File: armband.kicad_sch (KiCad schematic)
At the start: 35 parts, among them IC1 STM32MP157AAB3, IC7 S40FC004C1B2C00000, IC9 NXS0506UPZ, J2 Conn_01x02, J3 MEM2075-00-140-01-A, SW1 SW_MEC_5G, SW2 SW_MEC_5G

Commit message: first power management layout iteration, added footprints and values to parts that had none
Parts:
- C1, C2: footprint Capacitor_SMD:C_0603_1608Metric -> Capacitor_SMD:C_0402_1005Metric
- C27, C28, C66: footprint (none) -> Capacitor_SMD:C_0402_1005Metric
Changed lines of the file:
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@@
       (effects (font (size 1.27 1.27)) (justify left))
     )
-    (property "Footprint" "" (at 344.17 86.36 0)
+    (property "Footprint" "Capacitor_SMD:C_0402_1005Metric" (at 344.17 86.36 0)
       (effects (font (size 1.27 1.27)) hide)
     )
@@
       (effects (font (size 1.27 1.27)) (justify left))
     )
-    (property "Footprint" "" (at 394.97 121.92 0)
+    (property "Footprint" "Capacitor_SMD:C_0402_1005Metric" (at 394.97 121.92 0)
       (effects (font (size 1.27 1.27)) hide)
     )
@@
       (effects (font (size 1.27 1.27)) (justify left))
     )
-    (property "Footprint" "Capacitor_SMD:C_0603_1608Metric" (at 294.64 46.99 0)
+    (property "Footprint" "Capacitor_SMD:C_0402_1005Metric" (at 294.64 46.99 0)
       (effects (font (size 1.27 1.27)) hide)
     )
@@
       (effects (font (size 1.27 1.27)) (justify left))
     )
-    (property "Footprint" "Capacitor_SMD:C_0603_1608Metric" (at 318.77 46.99 0)
+    (property "Footprint" "Capacitor_SMD:C_0402_1005Metric" (at 318.77 46.99 0)
       (effects (font (size 1.27 1.27)) hide)
     )
@@
       (effects (font (size 1.27 1.27)) (justify left))
     )
-    (property "Footprint" "" (at 392.43 55.88 0)
+    (property "Footprint" "Capacitor_SMD:C_0402_1005Metric" (at 392.43 55.88 0)
       (effects (font (size 1.27 1.27)) hide)
     )
@@
   )
   (symbol (lib_id "ARMband:S40FC004C1B2C00000") (at 384.81 34.29 0) (unit 1)
-    (in_bom yes) (on_board no) (dnp yes) (fields_autoplaced)
+    (in_bom yes) (on_board yes) (dnp yes) (fields_autoplaced)
     (property "Reference" "IC7" (at 364.49 27.5209 0)
       (effects (font (size 1.27 1.27)))

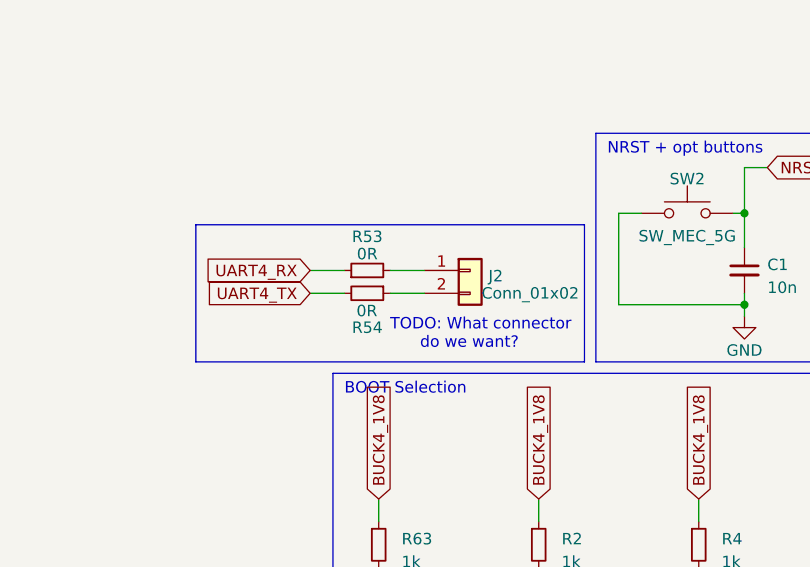
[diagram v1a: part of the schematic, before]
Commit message: Add missing footprints to components
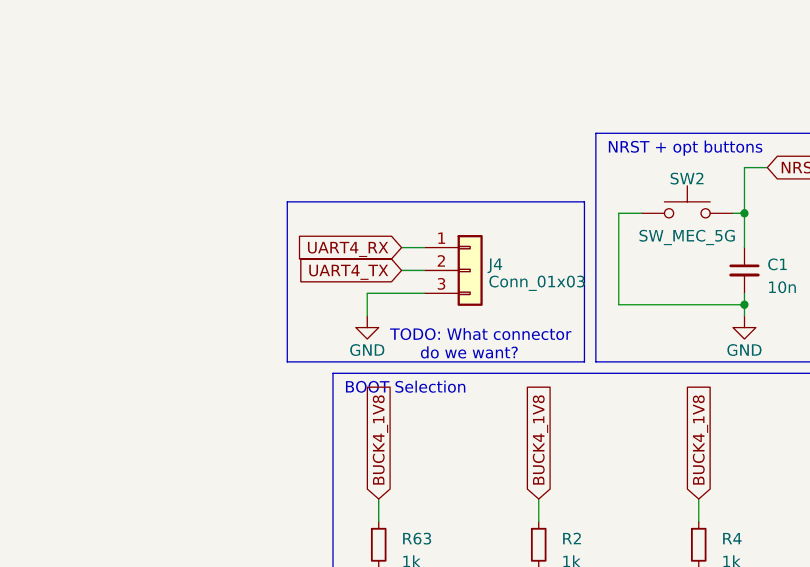
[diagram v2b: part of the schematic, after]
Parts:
- removed J2: Conn_01x02, symbol Connector_Generic:Conn_01x02
- removed R53, R54: 0R, Resistor_SMD:R_0201_0603Metric_Pad0.64x0.40mm_HandSolder, symbol Device:R_Small
- added J4: Conn_01x03, Connector_PinHeader_2.54mm:PinHeader_1x03_P2.54mm_Vertical, symbol Connector_Generic:Conn_01x03
- R55: footprint (none) -> Resistor_SMD:R_0402_1005Metric
- SW1, SW2: footprint (none) -> ARMband:SW-SMD_4P-L2.6-W1.6-P0.75-LS3.0; LCSC (none) -> C913778
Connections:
- net GND: now also J4.3 (Pin_3)
- net UART4_RX: now also J4.1 (Pin_1)
- net UART4_TX: now also J4.2 (Pin_2)
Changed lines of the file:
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@@
     (stroke (width 0) (type default))
   )
-  (wire (pts (xy 255.27 49.53) (xy 259.08 49.53))
-    (stroke (width 0) (type default))
-  )
-  (wire (pts (xy 246.38 46.99) (xy 250.19 46.99))
-    (stroke (width 0) (type default))
-  )
   (polyline (pts (xy 278.13 31.75) (xy 328.93 31.75))
     (stroke (width 0) (type default))
@@
     (stroke (width 0) (type default))
   )
-  (wire (pts (xy 255.27 46.99) (xy 259.08 46.99))
+  (wire (pts (xy 256.54 44.45) (xy 259.08 44.45))
     (stroke (width 0) (type default))
   )
@@
     (stroke (width 0) (type default))
   )
-  (wire (pts (xy 246.38 49.53) (xy 250.19 49.53))
+  (wire (pts (xy 256.54 46.99) (xy 259.08 46.99))
     (stroke (width 0) (type default))
   )
@@
     (stroke (width 0) (type default))
   )
+  (wire (pts (xy 252.73 49.53) (xy 252.73 52.07))
+    (stroke (width 0) (type default))
+  )
   (wire (pts (xy 384.81 67.31) (xy 384.81 69.85))
     (stroke (width 0) (type default))
@@
     (stroke (width 0) (type default))
   )
+  (wire (pts (xy 259.08 49.53) (xy 252.73 49.53))
+    (stroke (width 0) (type default))
+  )
   (wire (pts (xy 332.74 113.03) (xy 332.74 128.27))
     (stroke (width 0) (type default))
@@
     (fill (type none))
   )
-  (rectangle (start 233.68 41.91) (end 276.86 57.15)
+  (rectangle (start 243.84 39.37) (end 276.86 57.15)
     (stroke (width 0) (type default))
     (fill (type none))
@@
     (effects (font (size 1.27 1.27)) (justify left bottom))
   )
-  (text "TODO: What connector\n      do we want?" (at 255.27 55.88 0)
+  (text "TODO: What connector\n      do we want?" (at 255.27 57.15 0)
     (effects (font (size 1.27 1.27)) (justify left bottom))
   )
@@
     )
   )
-  (global_label "UART4_RX" (shape input) (at 246.38 46.99 180) (fields_autoplaced)
+  (global_label "UART4_RX" (shape input) (at 256.54 44.45 180) (fields_autoplaced)
     (effects (font (size 1.27 1.27)) (justify right))
-    (property "Intersheetrefs" "${INTERSHEET_REFS}" (at 234.1609 46.99 0)
+    (property "Intersheetrefs" "${INTERSHEET_REFS}" (at 244.3209 44.45 0)
       (effects (font (size 1.27 1.27)) (justify right) hide)
     )
@@
     )
   )
-  (global_label "UART4_TX" (shape input) (at 246.38 49.53 180) (fields_autoplaced)
+  (global_label "UART4_TX" (shape input) (at 256.54 46.99 180) (fields_autoplaced)
     (effects (font (size 1.27 1.27)) (justify right))
-    (property "Intersheetrefs" "${INTERSHEET_REFS}" (at 234.4633 49.53 0)
+    (property "Intersheetrefs" "${INTERSHEET_REFS}" (at 244.6233 46.99 0)
       (effects (font (size 1.27 1.27)) (justify right) hide)
     )
@@
       (effects (font (size 1.27 1.27)))
     )
-    (property "Footprint" "" (at 346.71 134.62 0)
+    (property "Footprint" "Resistor_SMD:R_0402_1005Metric" (at 346.71 134.62 0)
       (effects (font (size 1.27 1.27)) hide)
     )
@@
     )
   )
+  (symbol (lib_id "Connector_Generic:Conn_01x03") (at 264.16 46.99 0) (unit 1)
+    (in_bom yes) (on_board yes) (dnp no) (fields_autoplaced)
+    (property "Reference" "J4" (at 266.192 46.3463 0)
+      (effects (font (size 1.27 1.27)) (justify left))
+    )
+    (property "Value" "Conn_01x03" (at 266.192 48.2673 0)
+      (effects (font (size 1.27 1.27)) (justify left))
+    )
+    (property "Footprint" "Connector_PinHeader_2.54mm:PinHeader_1x03_P2.54mm_Vertical" (at 264.16 46.99 0)
+      (effects (font (size 1.27 1.27)) hide)
+    )
+    (property "Datasheet" "~" (at 264.16 46.99 0)
+      (effects (font (size 1.27 1.27)) hide)
+    )
+    (pin "1")
+    (pin "2")
+    (pin "3")
+    (instances
+      (project "armband"
+        (path "/017c50c6-333c-4d31-ad5a-278994a09b14"
+          (reference "J4") (unit 1)
+        )
+      )
+    )
+  )
   (symbol (lib_id "Device:R_Small") (at 36.83 62.23 90) (unit 1)
     (in_bom yes) (on_board yes) (dnp no)
@@
       (effects (font (size 1.27 1.27)))
     )
-    (property "Footprint" "" (at 312.42 35.56 0)
+    (property "Footprint" "ARMband:SW-SMD_4P-L2.6-W1.6-P0.75-LS3.0" (at 312.42 35.56 0)
       (effects (font (size 1.27 1.27)) hide)
     )
@@
       (effects (font (size 1.27 1.27)) hide)
     )
+    (property "LCSC" "C913778" (at 312.42 40.64 0)
+      (effects (font (size 1.27 1.27)) hide)
+    )
     (pin "1")
     (pin "3")
@@
     )
   )
-  (symbol (lib_id "Connector_Generic:Conn_01x02") (at 264.16 46.99 0) (unit 1)
-    (in_bom yes) (on_board yes) (dnp no)
-    (property "Reference" "J2" (at 266.192 47.6163 0)
-      (effects (font (size 1.27 1.27)) (justify left))
-    )
-    (property "Value" "Conn_01x02" (at 265.43 49.53 0)
-      (effects (font (size 1.27 1.27)) (justify left))
-    )
-    (property "Footprint" "" (at 264.16 46.99 0)
-      (effects (font (size 1.27 1.27)) hide)
-    )
-    (property "Datasheet" "~" (at 264.16 46.99 0)
-      (effects (font (size 1.27 1.27)) hide)
-    )
-    (pin "1")
-    (pin "2")
-    (instances
-      (project "armband"
-        (path "/017c50c6-333c-4d31-ad5a-278994a09b14"
-          (reference "J2") (unit 1)
-        )
-      )
-    )
-  )
   (symbol (lib_id "Device:C_Small") (at 318.77 46.99 0) (unit 1)
     (in_bom yes) (on_board yes) (dnp no) (fields_autoplaced)
@@
     )
   )
+  (symbol (lib_name "GND_1") (lib_id "power:GND") (at 252.73 52.07 0) (mirror y) (unit 1)
+    (in_bom yes) (on_board yes) (dnp no)
+    (property "Reference" "#PWR01" (at 252.73 58.42 0)
+      (effects (font (size 1.27 1.27)) hide)
+    )
+    (property "Value" "GND" (at 252.73 55.88 0)
+      (effects (font (size 1.27 1.27)))
+    )
+    (property "Footprint" "" (at 252.73 52.07 0)
+      (effects (font (size 1.27 1.27)) hide)
+    )
+    (property "Datasheet" "" (at 252.73 52.07 0)
+      (effects (font (size 1.27 1.27)) hide)
+    )
+    (pin "1")
+    (instances
+      (project "armband"
+        (path "/017c50c6-333c-4d31-ad5a-278994a09b14/5731d22b-18c2-4920-9f80-2a6ce209edf2"
+          (reference "#PWR01") (unit 1)
+        )
+        (path "/017c50c6-333c-4d31-ad5a-278994a09b14"
+          (reference "#PWR066") (unit 1)
+        )
+      )
+    )
+  )
   (symbol (lib_id "Device:R_Small") (at 254 87.63 0) (unit 1)
     (in_bom yes) (on_board yes) (dnp no) (fields_autoplaced)
@@
       (effects (font (size 1.27 1.27)))
     )
-    (property "Footprint" "" (at 288.29 35.56 0)
+    (property "Footprint" "ARMband:SW-SMD_4P-L2.6-W1.6-P0.75-LS3.0" (at 288.29 35.56 0)
       (effects (font (size 1.27 1.27)) hide)
     )
@@
       (effects (font (size 1.27 1.27)) hide)
     )
+    (property "LCSC" "C913778" (at 288.29 40.64 0)
+      (effects (font (size 1.27 1.27)) hide)
+    )
     (pin "1")
     (pin "3")
@@
     )
   )
-  (symbol (lib_id "Device:R_Small") (at 252.73 49.53 270) (unit 1)
-    (in_bom yes) (on_board yes) (dnp no)
-    (property "Reference" "R54" (at 252.73 53.34 90)
-      (effects (font (size 1.27 1.27)))
-    )
-    (property "Value" "0R" (at 252.6899 51.4872 90)
-      (effects (font (size 1.27 1.27)))
-    )
-    (property "Footprint" "Resistor_SMD:R_0201_0603Metric_Pad0.64x0.40mm_HandSolder" (at 252.73 49.53 0)
-      (effects (font (size 1.27 1.27)) hide)
-    )
-    (property "Datasheet" "~" (at 252.73 49.53 0)
-      (effects (font (size 1.27 1.27)) hide)
-    )
-    (property "MFN" "" (at 252.73 49.53 0)
-      (effects (font (size 1.27 1.27)) hide)
-    )
-    (pin "1")
-    (pin "2")
-    (instances
-      (project "armband"
-        (path "/017c50c6-333c-4d31-ad5a-278994a09b14"
-          (reference "R54") (unit 1)
-        )
-      )
-    )
-  )
   (symbol (lib_id "Device:R_Small") (at 313.69 83.82 0) (mirror y) (unit 1)
     (in_bom yes) (on_board yes) (dnp no)
@@
         )
       )
-    )
-  )
-  (symbol (lib_id "Device:R_Small") (at 252.73 46.99 90) (unit 1)
-    (in_bom yes) (on_board yes) (dnp no) (fields_autoplaced)
-    (property "Reference" "R53" (at 252.73 43.2435 90)
-      (effects (font (size 1.27 1.27)))
-    )
-    (property "Value" "0R" (at 252.73 45.1645 90)
-      (effects (font (size 1.27 1.27)))
-    )
-    (property "Footprint" "Resistor_SMD:R_0201_0603Metric_Pad0.64x0.40mm_HandSolder" (at 252.73 46.99 0)
-      (effects (font (size 1.27 1.27)) hide)
-    )
-    (property "Datasheet" "~" (at 252.73 46.99 0)
-      (effects (font (size 1.27 1.27)) hide)
-    )
-    (property "MFN" "" (at 252.73 46.99 0)
-      (effects (font (size 1.27 1.27)) hide)
-    )
-    (pin "1")
-    (pin "2")
-    (instances
-      (project "armband"
-        (path "/017c50c6-333c-4d31-ad5a-278994a09b14"
-          (reference "R53") (unit 1)
-        )
-      )

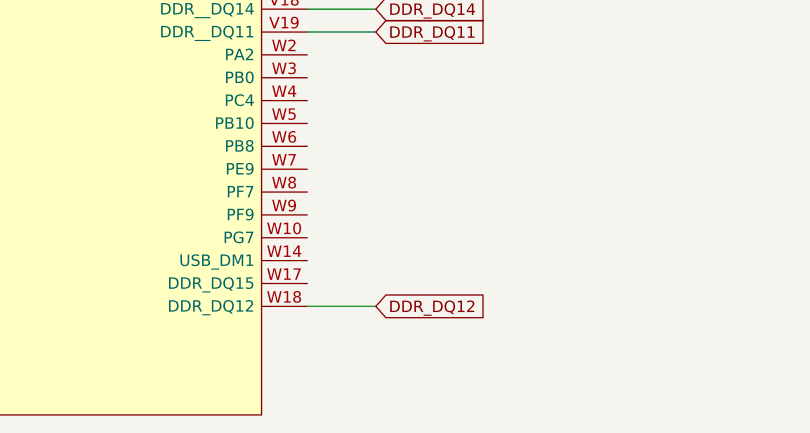
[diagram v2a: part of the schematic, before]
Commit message: reworked RAM
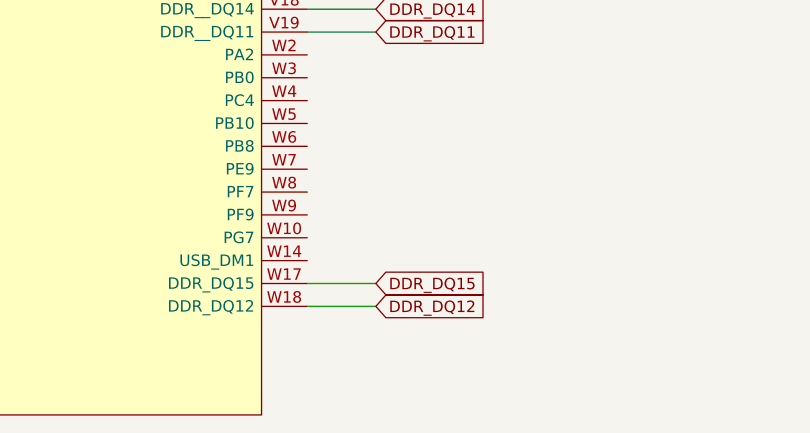
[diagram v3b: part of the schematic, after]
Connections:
- net DDR_DQ15: now reaches IC1.W17 (DDR_DQ15)
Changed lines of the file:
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@@
+    (stroke (width 0) (type default))
+  )
+  (wire (pts (xy 146.05 259.08) (xy 153.67 259.08))
     (stroke (width 0) (type default))
   )
@@
     )
   )
+  (global_label "DDR_DQ15" (shape input) (at 153.67 259.08 0) (fields_autoplaced)
+    (effects (font (size 1.27 1.27)) (justify left))
+    (property "Intersheetrefs" "${INTERSHEET_REFS}" (at 166.3729 259.08 0)
+      (effects (font (size 1.27 1.27)) (justify left) hide)
+    )
+  )

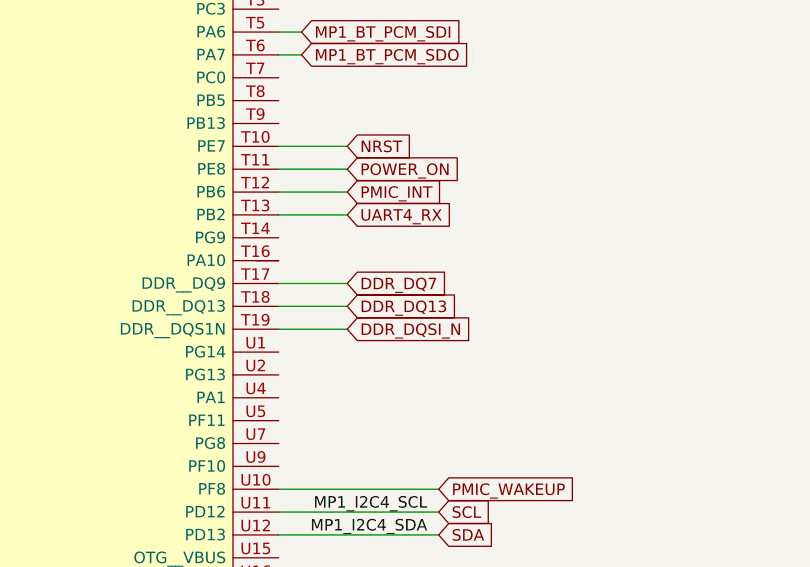
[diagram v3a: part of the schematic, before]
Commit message: Fix RAM Labels
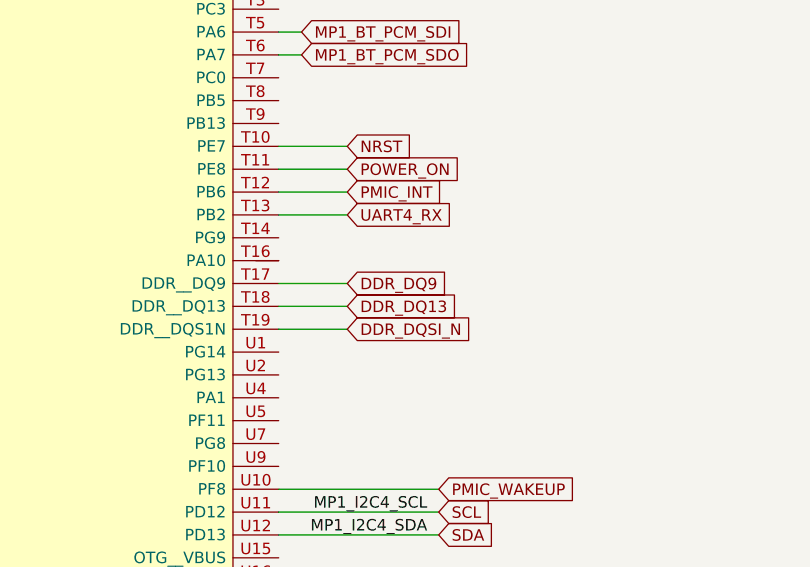
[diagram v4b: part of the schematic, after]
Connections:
- net DDR_DQ7: no longer IC1.T17 (DDR__DQ9)
- new net DDR_DQ9: IC1.T17 (DDR__DQ9)
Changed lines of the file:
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@@
     )
   )
-  (global_label "DDR_DQ7" (shape input) (at 153.67 154.94 0) (fields_autoplaced)
+  (global_label "DDR_DQ9" (shape input) (at 153.67 154.94 0) (fields_autoplaced)
     (effects (font (size 1.27 1.27)) (justify left))
     (property "Intersheetrefs" "${INTERSHEET_REFS}" (at 165.1634 154.94 0)

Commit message: added flash
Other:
- added sheet flash (flash.kicad_sch)
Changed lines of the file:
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@@
+    )
+  )
+  (sheet (at 299.72 222.25) (size 25.4 12.7) (fields_autoplaced)
+    (stroke (width 0.1524) (type solid))
+    (fill (color 0 0 0 0.0000))
+    (property "Sheetname" "flash" (at 299.72 221.5384 0)
+      (effects (font (size 1.27 1.27)) (justify left bottom))
+    )
+    (property "Sheetfile" "flash.kicad_sch" (at 299.72 235.5346 0)
+      (effects (font (size 1.27 1.27)) (justify left top))
+    )
+    (instances
+      (project "armband"
+        (path "/017c50c6-333c-4d31-ad5a-278994a09b14" (page "5"))
+      )
     )
   )
